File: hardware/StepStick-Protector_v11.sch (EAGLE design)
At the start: 15 parts, among them IC1 STEPSTICK-TP, J1 JUMPER2-0603-NC, X1 PASSER, X2 PASSER

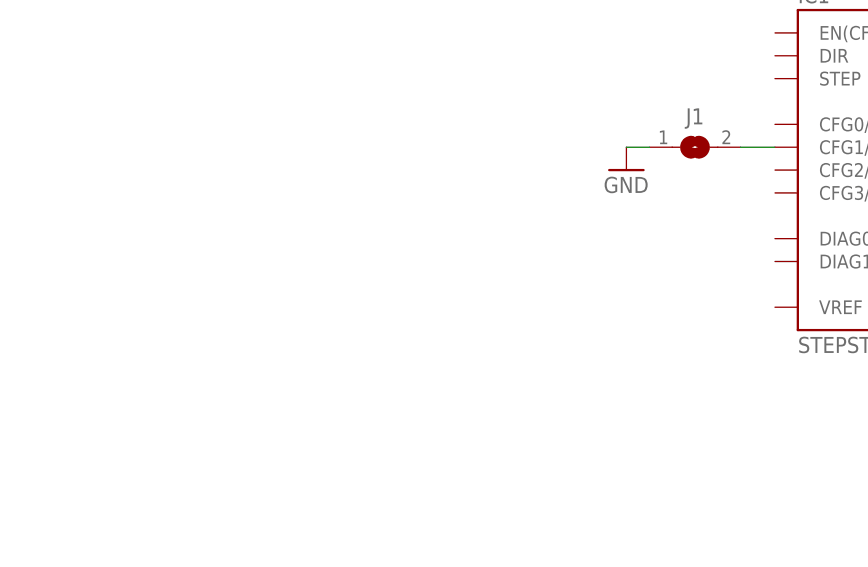
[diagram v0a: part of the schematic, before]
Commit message: updated schematics
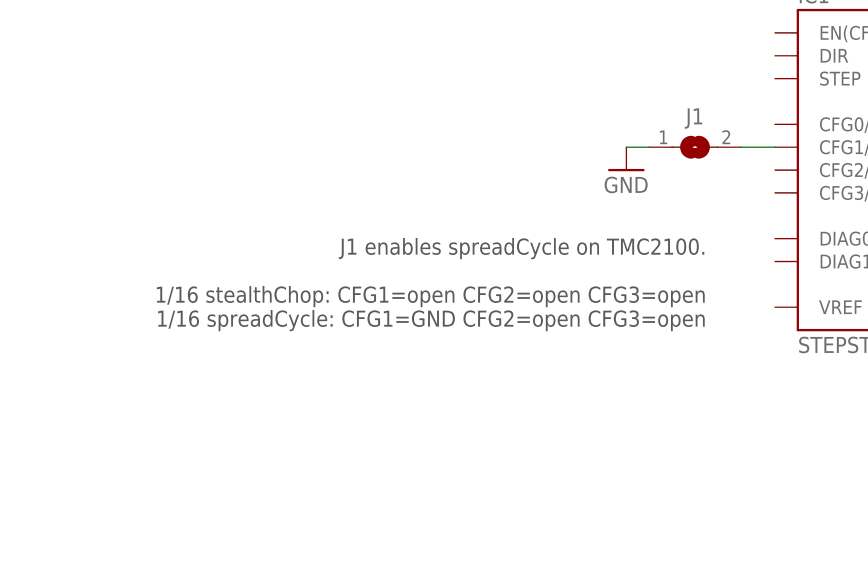
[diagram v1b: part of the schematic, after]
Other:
- note added: "J1 enables spreadCycle on TMC2100. 1/16 stealthChop: CFG1=open CFG2=open CFG3=open 1/16 spreadCycle: CFG1=GND CFG2=open CFG3=open"
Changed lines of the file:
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@@
 <text x="162.56" y="15.24" size="1.27" layer="95">Designed by Andreas Watterott (Watterott electronic)</text>
 <text x="162.56" y="83.82" size="1.778" layer="97" align="center">Schottky Diodes 2A/60V</text>
+<text x="83.82" y="93.98" size="1.778" layer="97" align="top-right">J1 enables spreadCycle on TMC2100.
+1/16 stealthChop: CFG1=open CFG2=open CFG3=open
+1/16 spreadCycle: CFG1=GND CFG2=open CFG3=open</text>
 </plain>
 <instances>
@@
 </schematic>
 </drawing>
+<compatibility>
+<note version="6.3" minversion="6.2.2" severity="warning">
+Since Version 6.2.2 text objects can contain more than one line,
+which will not be processed correctly with this version.
+</note>
+</compatibility>
 </eagle>

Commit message: updated schematics and layout files
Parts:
- D1+, D1-, D2+, D2-, D3+, D3-, D4+, D4-: value (none) -> S310FA; device we-rcl:D_SCHOTTKY-SMA -> we-rcl:D_SCHOTTKY-SOD123
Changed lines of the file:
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@@
 <part name="FRAME1" library="we-symbol" deviceset="FRAME-A4L" device=""/>
 <part name="IC1" library="we-board" deviceset="STEPSTICK" device="-TP"/>
-<part name="D1+" library="we-rcl" deviceset="D_SCHOTTKY" device="-SMA"/>
-<part name="D2+" library="we-rcl" deviceset="D_SCHOTTKY" device="-SMA"/>
-<part name="D3+" library="we-rcl" deviceset="D_SCHOTTKY" device="-SMA"/>
-<part name="D4+" library="we-rcl" deviceset="D_SCHOTTKY" device="-SMA"/>
-<part name="D1-" library="we-rcl" deviceset="D_SCHOTTKY" device="-SMA"/>
-<part name="D2-" library="we-rcl" deviceset="D_SCHOTTKY" device="-SMA"/>
-<part name="D3-" library="we-rcl" deviceset="D_SCHOTTKY" device="-SMA"/>
-<part name="D4-" library="we-rcl" deviceset="D_SCHOTTKY" device="-SMA"/>
+<part name="D1+" library="we-rcl" deviceset="D_SCHOTTKY" device="-SOD123" value="S310FA"/>
+<part name="D2+" library="we-rcl" deviceset="D_SCHOTTKY" device="-SOD123" value="S310FA"/>
+<part name="D3+" library="we-rcl" deviceset="D_SCHOTTKY" device="-SOD123" value="S310FA"/>
+<part name="D4+" library="we-rcl" deviceset="D_SCHOTTKY" device="-SOD123" value="S310FA"/>
+<part name="D1-" library="we-rcl" deviceset="D_SCHOTTKY" device="-SOD123" value="S310FA"/>
+<part name="D2-" library="we-rcl" deviceset="D_SCHOTTKY" device="-SOD123" value="S310FA"/>
+<part name="D3-" library="we-rcl" deviceset="D_SCHOTTKY" device="-SOD123" value="S310FA"/>
+<part name="D4-" library="we-rcl" deviceset="D_SCHOTTKY" device="-SOD123" value="S310FA"/>
 <part name="GND1" library="supply1" deviceset="GND" device=""/>
 <part name="P+1" library="supply1" deviceset="V+" device="" value="VM"/>
@@
 <text x="162.56" y="15.24" size="1.27" layer="95">Designed by Andreas Watterott (Watterott electronic)</text>
 <text x="162.56" y="83.82" size="1.778" layer="97" align="center">Schottky Diodes 2A/60V</text>
-<text x="83.82" y="93.98" size="1.778" layer="97" align="top-right">J1 enables spreadCycle on TMC2100.
+<text x="83.82" y="91.44" size="1.778" layer="97" align="top-right">J1 enables spreadCycle on TMC2100.
 1/16 stealthChop: CFG1=open CFG2=open CFG3=open
 1/16 spreadCycle: CFG1=GND CFG2=open CFG3=open</text>
